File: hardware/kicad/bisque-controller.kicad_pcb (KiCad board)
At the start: 2 copper layers, 100 x 80 mm, 49 parts, among them J1 USB-C, J2 5V_IN, J3 TC_K, J4 SSR, J5 DISPLAY, J6 NAV_SW, J7 AUX, Q1 AO3400A, Q2 AO3400A, SW1 RESET, SW2 BOOT, U1 ESP32-S3-WROOM-1-N16R8, U2 AMS1117-3.3, U3 MAX31855KASA+, U4 USBLC6-2SC6

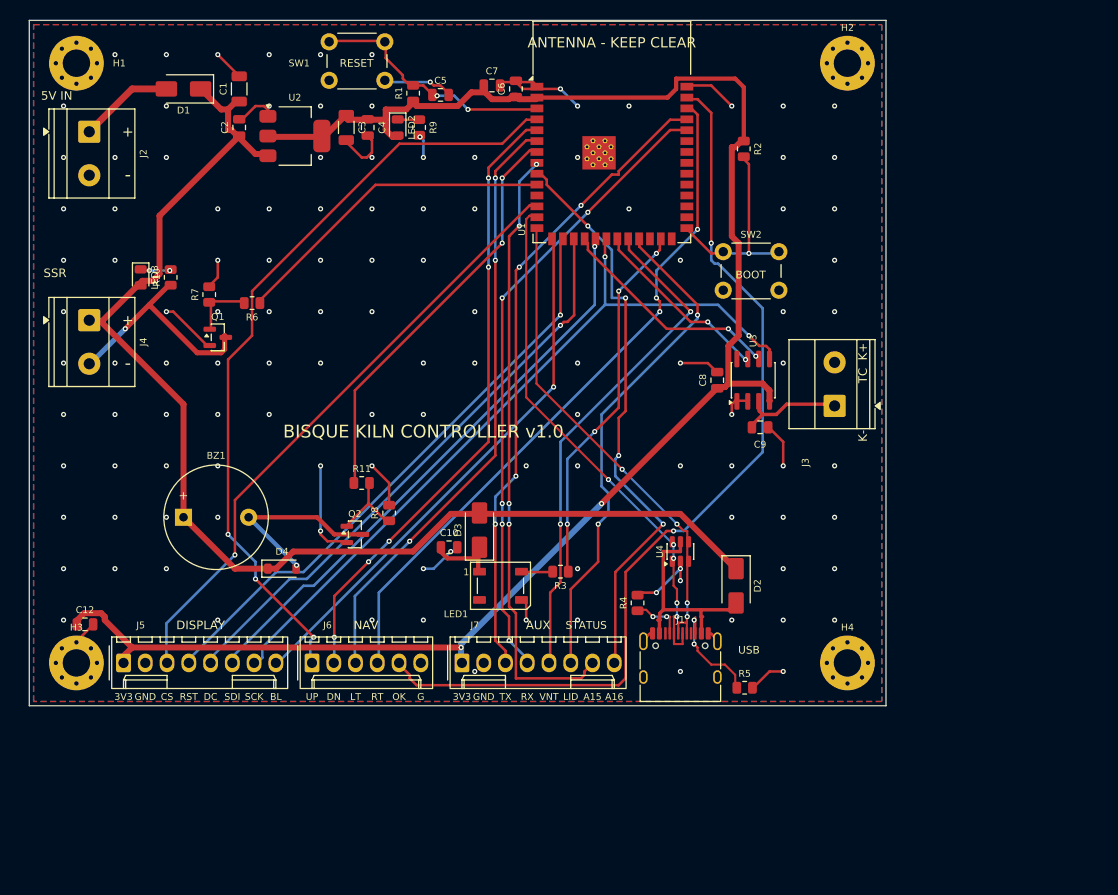
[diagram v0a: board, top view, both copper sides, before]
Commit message: hardware: move display to +5V power, correct 3.5"->4.0" everywhere
Switches the KiCad PCB's display header (J5) from +3V3 to +5V power, per
the user's own hardware: a 4.0" LCDWIKI ST7796S module (MSP4020/MSP4021),
not the 3.5" panel this project previously assumed.

design.py: J5 pin 1 and its local decoupling cap C12 move from +3V3 to
+5V. Verified pin-compatible against the module's own manual (LCDWiki's
product page returned only marketing copy; the linked PDF is a 24-page
scan with no embedded fonts, so it had to be rendered and read directly) -
pins 1-8 are VCC/GND/CS/RESET/DC/SDI/SCK/LED, an exact match for J5's
existing assignment, and VCC is rated 3.3-5V with every reference wiring
diagram in the manual (including 3.3V-logic MCU boards) tying VCC to 5V
while driving the SPI pins directly, no level shifter. No connector or
firmware change needed - same resolution, same driver IC, same GPIOs.

This is the real fix for the AMS1117 (U2) thermal margin flagged in the
prior fab review: the display's backlight and panel logic were the
dominant load the schematic analyzer's power budget never accounted for
(it only sums ICs on a rail). Moving that load to +5V drops U2 back to
just the ESP32 + MAX31855 (~245mA), which keeps its junction temperature
under the datasheet's 125C limit even at a hot enclosure ambient - more
effective than the ground-pour mitigation the prior review proposed.

Rebuilding after the net rename surfaced a real DRC regression: reshaping
+3V3/+5V's routing left one of 197 decorative GND stitching vias isolated
from copper on one layer, a failure mode heal_islands() doesn't cover (it
only bridges pour islands lacking a via, not a via sitting in a clearance
gap). Added drop_disconnected_stitch_vias() to kicad_build.py - safe by
construction, since GND has no point-to-point routing, so every GND via
is decorative and dropping one never touches a real signal connection.
Verified deterministic across rebuilds; DRC is back to 0 errors/0
unconnected a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
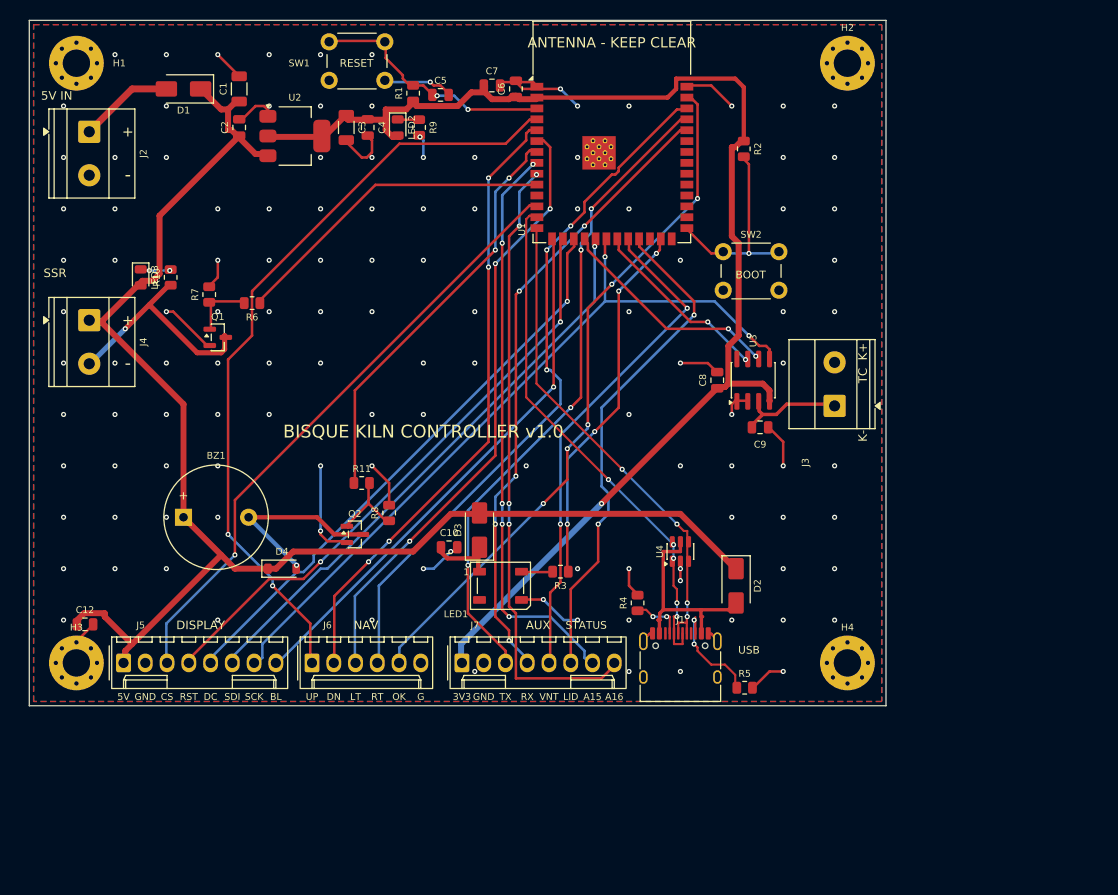
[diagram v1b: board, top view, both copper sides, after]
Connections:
- C12 pad 1: +3V3 -> +5V
- J5 pad 1: +3V3 -> +5V
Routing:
- net +3V3: track 206.6 -> 156.4 mm, vias 2 -> 1
- net +5V: track 144.4 -> 171.1 mm
- net BTN_SEL: track 108.1 -> 81.5 mm, vias 2 -> 5
- net AUX_B: track 68.0 -> 72.8 mm
- net AUX_A: track 71.5 -> 67.6 mm, vias 4 -> 5
- net GND: track 116.4 -> 118.8 mm, vias 121 -> 122
- net TXD0: track 75.1 -> 76.6 mm
- net BTN_LEFT: track 70.8 -> 71.9 mm
- net LCD_DC: track 68.7 -> 67.7 mm
- net BTN_RIGHT: track 81.5 -> 82.3 mm
- net LCD_RST: track 69.7 -> 70.2 mm, vias 1 -> 2
- net BTN_UP: track 90.6 -> 90.3 mm, vias 3 -> 2
- net BTN_DOWN: track 72.9 -> 72.7 mm, vias 5 -> 4
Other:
- board text added: "5V"

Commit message: hardware: cut JLCPCB assembly cost, fix via-in-pad and GND island bugs
Prototype-quantity cost at JLCPCB is dominated by fixed fees, not the BOM
($9.83/board). The board was paying $30 in per-order feeder fees across 10
unique Extended parts, and its 7 through-hole parts forced the Standard
assembly tier ($25 setup) purely to place $1.53/board of connectors.

Cost changes:
- SW1/SW2 swap the 6 mm THT tactile switch for XKB TS-1187A (LCSC C318884),
  a JLCPCB *Basic* part: no feeder fee and it stays on the SMT line.
- The remaining 7 THT parts plus the WS2812B are marked hand-fitted in
  gen_jlc.py and dropped from BOM/CPL, with a new
  jlcpcb/hand-solder-parts.csv shopping list (LCSC + Mouser second source).

Net: 10 unique Extended parts -> 4, $30 -> $12 in feeder fees, and the
order drops from Standard to Economic assembly.

No addressable RGB LED at LCSC is Basic, and substituting discrete R/G/B is
worse (Extended anyway, thin stock, +2 GPIOs, status_led rewrite), so the
5050 is hand-fitted rather than replaced. Likewise no USB-C connector in the
LCSC catalog is Basic or Preferred — max saving from any swap is $0.114/board
against rerouting 9 hand-tuned escape polylines, so C165948 stays.

Bugs found and fixed along the way:
- router.py placed vias inside same-net SMD pads. Clearance rules ignore the
  same-net case and DRC never flags it, but an untented via in a pad wicks
  solder out of the joint during reflow. New VIA_PAD_GAP blocks it; new
  check_via_in_pad.py verifies it against pcbnew geometry (14 conflicts on
  the old board, 0 now).
- kicad_build.py heal_islands() only handled GND islands with no via at all,
  and counted signal vias as anchors. A group of islands that bridged to each
  other but never to the main pour passed the check while KiCad reported a
  missing Zone[GND]/Zone[GND] connection. Rewritten around union-find
  connectivity components.
- check_pcb.py squared circles to their bounding box, over-reporting
  circle-vs-rect distance by up 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
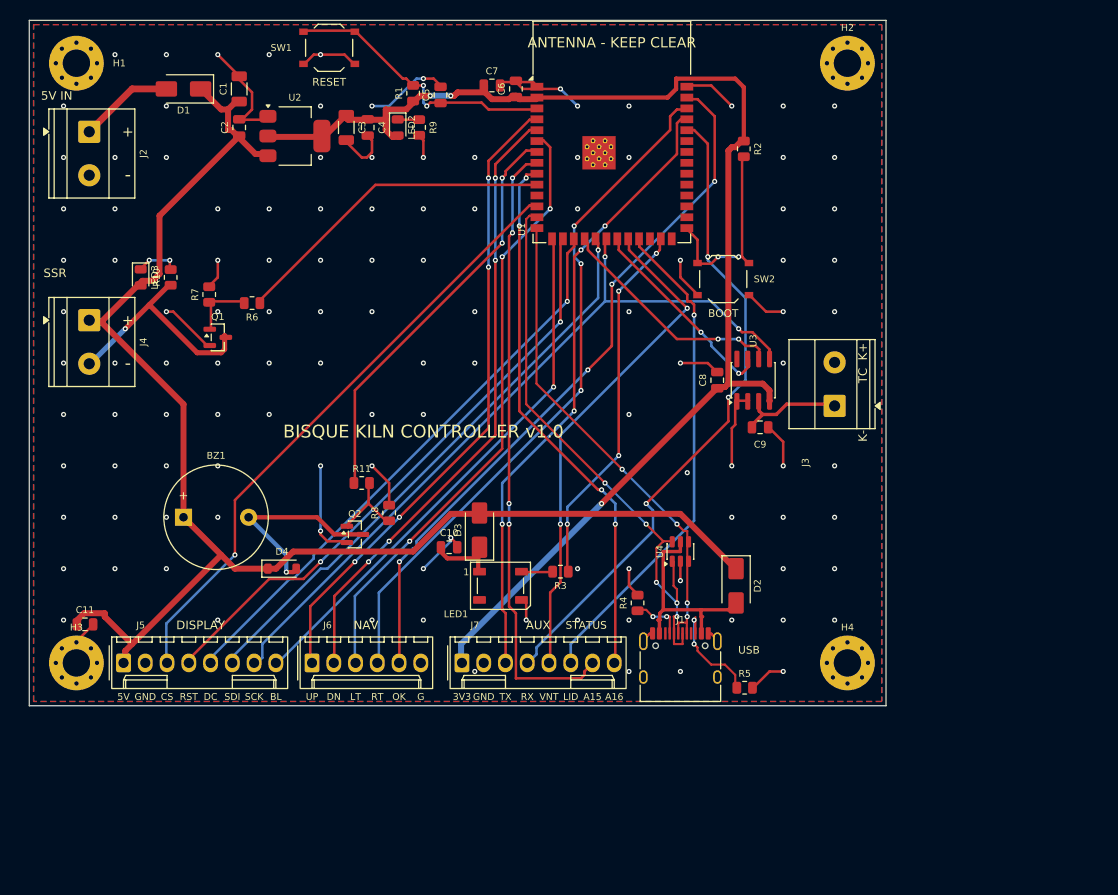
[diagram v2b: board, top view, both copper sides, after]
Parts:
- removed C12: 10uF, C_0805_2012Metric
- added C11: 10uF, C_0805_2012Metric, F.Cu at (26.5, 90.5)
- SW1, SW2: footprint SW_PUSH_6mm -> SW_Push_1P1T_XKB_TS-1187A
- moved SW2 3.20 mm to (101.0, 50.2)
- moved SW1 0.70 mm to (55.0, 23.2)
- turned C5 to 90 degrees
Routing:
- net GND: track 118.8 -> 145.4 mm, vias 122 -> 118
- net BTN_UP: track 90.3 -> 75.1 mm, vias 2 -> 4
- net AUX_B: track 72.8 -> 63.7 mm
- net USB_DN: track 62.0 -> 68.4 mm
- net AUX_A: track 67.6 -> 72.2 mm, vias 5 -> 4
- net EN: track 29.2 -> 32.9 mm
- net TXD0: track 76.6 -> 73.3 mm
- net RXD0: track 73.7 -> 77.0 mm, vias 5 -> 3
- net BTN_SEL: track 81.5 -> 83.7 mm, vias 5 -> 4
- net SPI_MISO: track 21.9 -> 23.9 mm
- net LEDS_K: track 3.84 -> 5.54 mm
- net BUZZ_K: track 22.5 -> 23.8 mm
- net BTN_RIGHT: track 82.3 -> 81.2 mm
- net IO0: track 24.1 -> 23.1 mm, vias 1 -> 2
- net +3V3: track 156.4 -> 155.4 mm, vias 1 -> 3
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
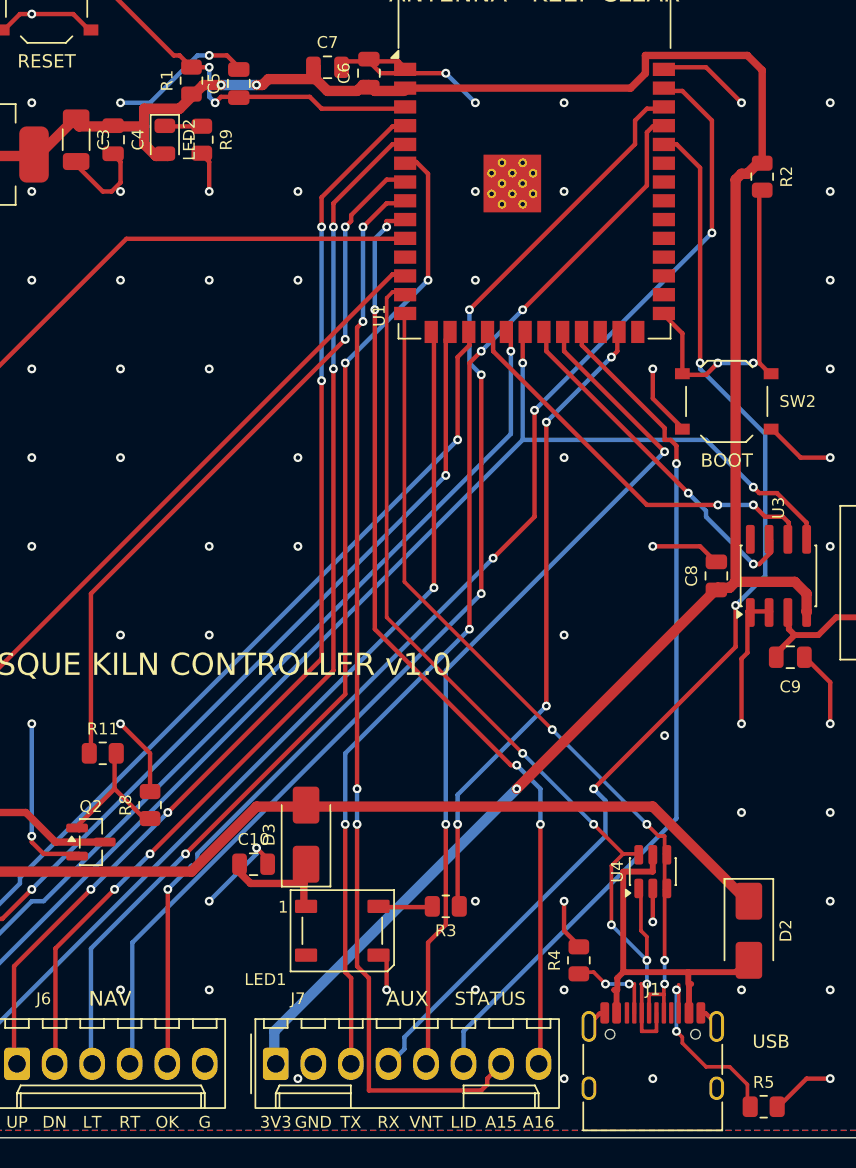
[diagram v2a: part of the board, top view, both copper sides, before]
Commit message: hardware: filter the lid-switch input for the #83 interlock
Firmware issue #83 turns the previously-unused lid/door switch
(CONFIG_KILN_PIN_LID_SWITCH, IO21) into a firing interlock. The board
already routed the net -- LID_SW on ESP32-S3 pin 23 to aux header J7 pin
6 -- but as a bare GPIO on the ESP32's weak ~45k internal pull-up. It is
the one input whose cable leaves the enclosure and runs to a hot kiln
lid alongside the SSR output and mains wiring, and once #83 lands a
false "lid open" cuts a firing, so noise immunity now matters.

J7 pin 6 becomes a new net LID_IN and reaches U1.23 (LID_SW) through:

  R12  1k 0805   series -- fault/ESD current limit + RC series element
  R13  10k 0805  pull-up to +3V3, replacing the internal one
  C12  100nF     shunt to GND at the point of entry

Why this combination rather than the alternatives:

- A bare external pull-up alone leaves the pin's own clamp diodes as the
  only transient path. Adding C12 costs one Basic part and gives a real
  low-pass: ~1.8 kHz with the switch closed (C12 across R12||R13 ~ 0.9k),
  ~160 Hz open. The firmware samples at 500 ms and debounces in software,
  so the RC only has to kill fast EMI transients, not bounce.
- R12 is needed anyway to form that RC and to limit fault current if the
  lid cable ever shorts to something. Closed-switch level is
  3.3V x 1k/11k = 0.30V, well under the ESP32's 0.25 x VDD (0.83V) V_IL.
- R13 at 10k rather than the internal ~45k so an open switch holds the
  node high against leakage and capacitive pickup on a long cable. It
  also matches the 10k parts already on the board (R1, R2, R7, R8).
- No discrete TVS. The board's only one is the USBLC6 (U4), fitted for
  USB 2.0's low-capacitance requirement; the other externally exposed
  nets (TC_P at J3, the nav switch at J6) rely on an RC plus the pin's
  clamp diodes. A TVS here would be inconsistent with the rest of the
  board and would add a unique Extended part ($3 feeder fee) for one
  input.

Assembly cost is un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
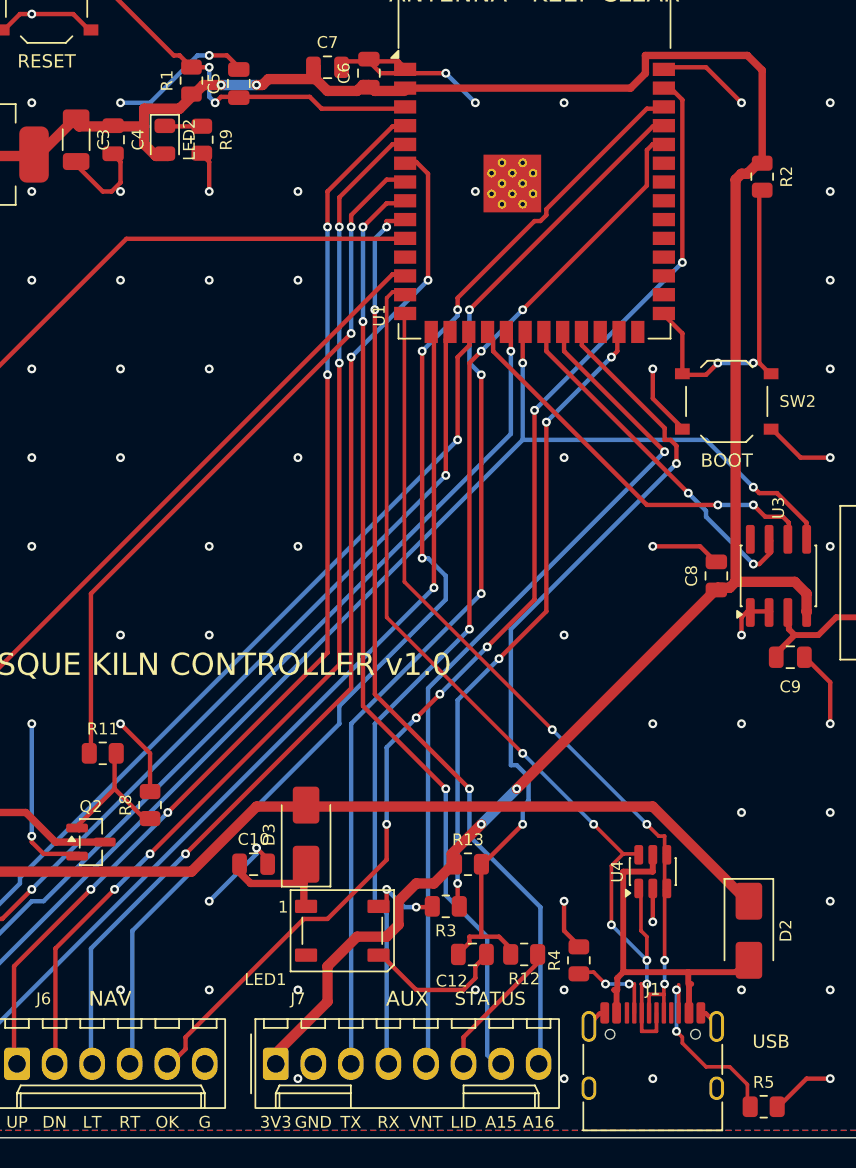
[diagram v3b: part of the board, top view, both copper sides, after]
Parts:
- added C12: 100nF, C_0805_2012Metric, F.Cu at (83.8, 87.6)
- added R12: 1k, R_0805_2012Metric, F.Cu at (87.3, 87.6)
- added R13: 10k, R_0805_2012Metric, F.Cu at (83.5, 81.5)
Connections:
- J7 pad 6: LID_SW -> LID_IN
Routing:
- net LID_IN: track 0.00 -> 9.94 mm
- net AUX_A: track 72.2 -> 64.3 mm, vias 4 -> 3
- net RXD0: track 77.0 -> 71.4 mm
- net LID_SW: track 58.6 -> 55.7 mm, vias 1 -> 2
- net +3V3: track 155.4 -> 157.5 mm, vias 3 -> 4
- net WS_DIN: track 3.76 -> 5.22 mm, vias 0 -> 2
- net BTN_SEL: track 83.7 -> 82.4 mm, vias 4 -> 6
- net GND: track 145.4 -> 146.5 mm, vias 118 -> 116
- net BTN_RIGHT: track 81.2 -> 82.3 mm
- net TXD0: track 73.3 -> 73.6 mm, vias 4 -> 3
- net AUX_B: track 63.7 -> 63.5 mm, vias 4 -> 3
- net VENT: vias 2 -> 1
